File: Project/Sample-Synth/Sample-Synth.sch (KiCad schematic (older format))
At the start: 0 parts

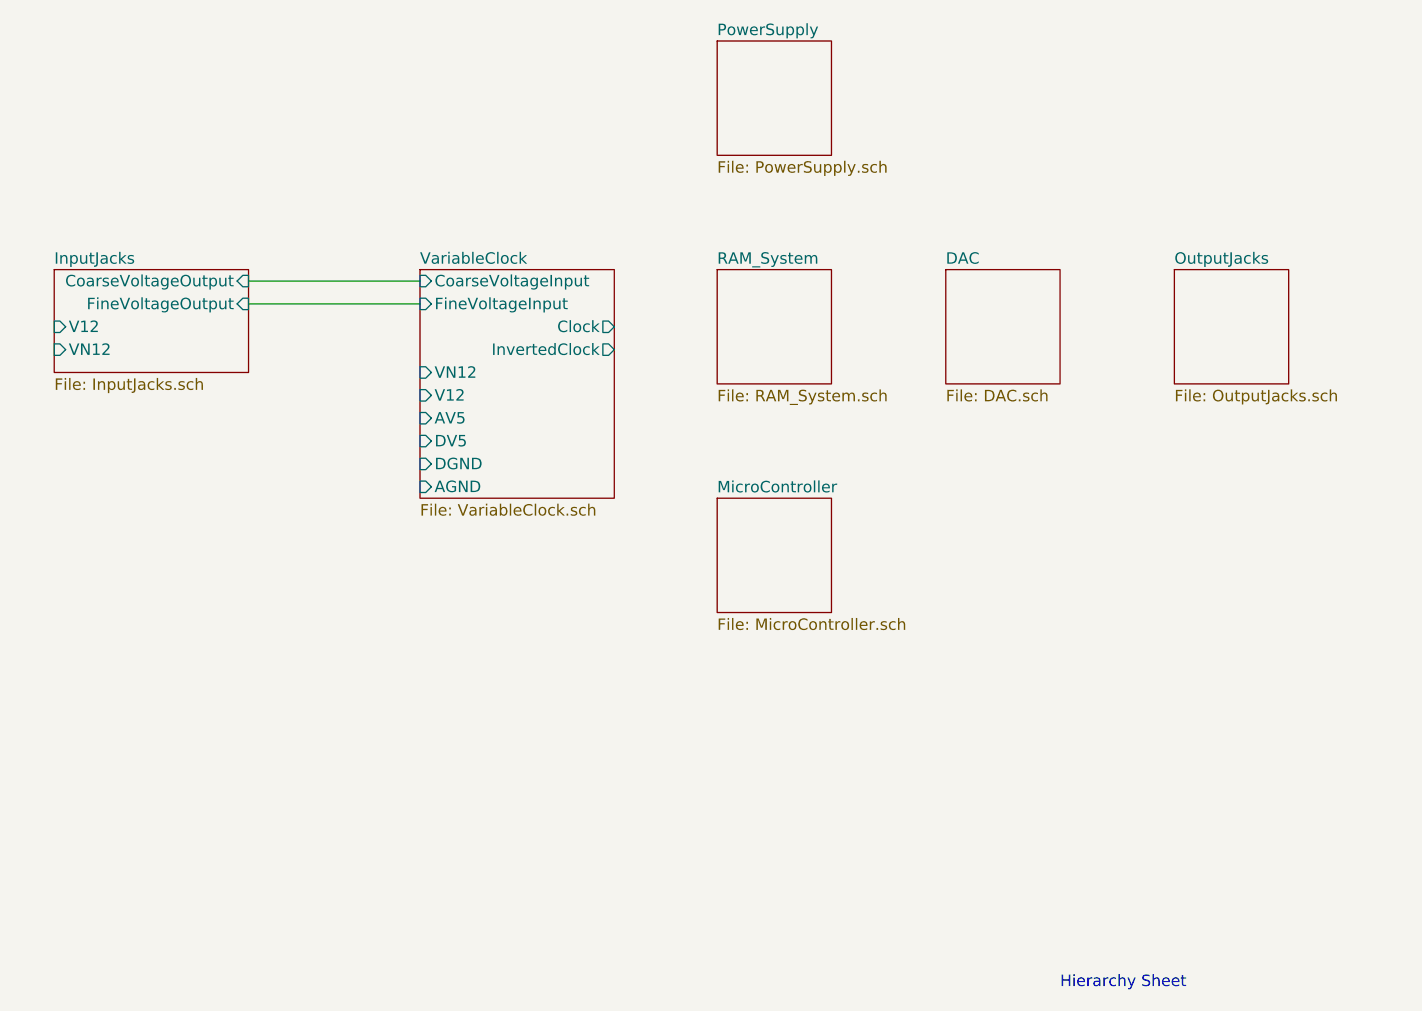
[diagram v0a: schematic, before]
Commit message: Updates to Schematic
Schematic updates: fixed connections on RAM, started setup for DAC stage.
Also swapped out the datasheet for the RAM to a more accurate one.
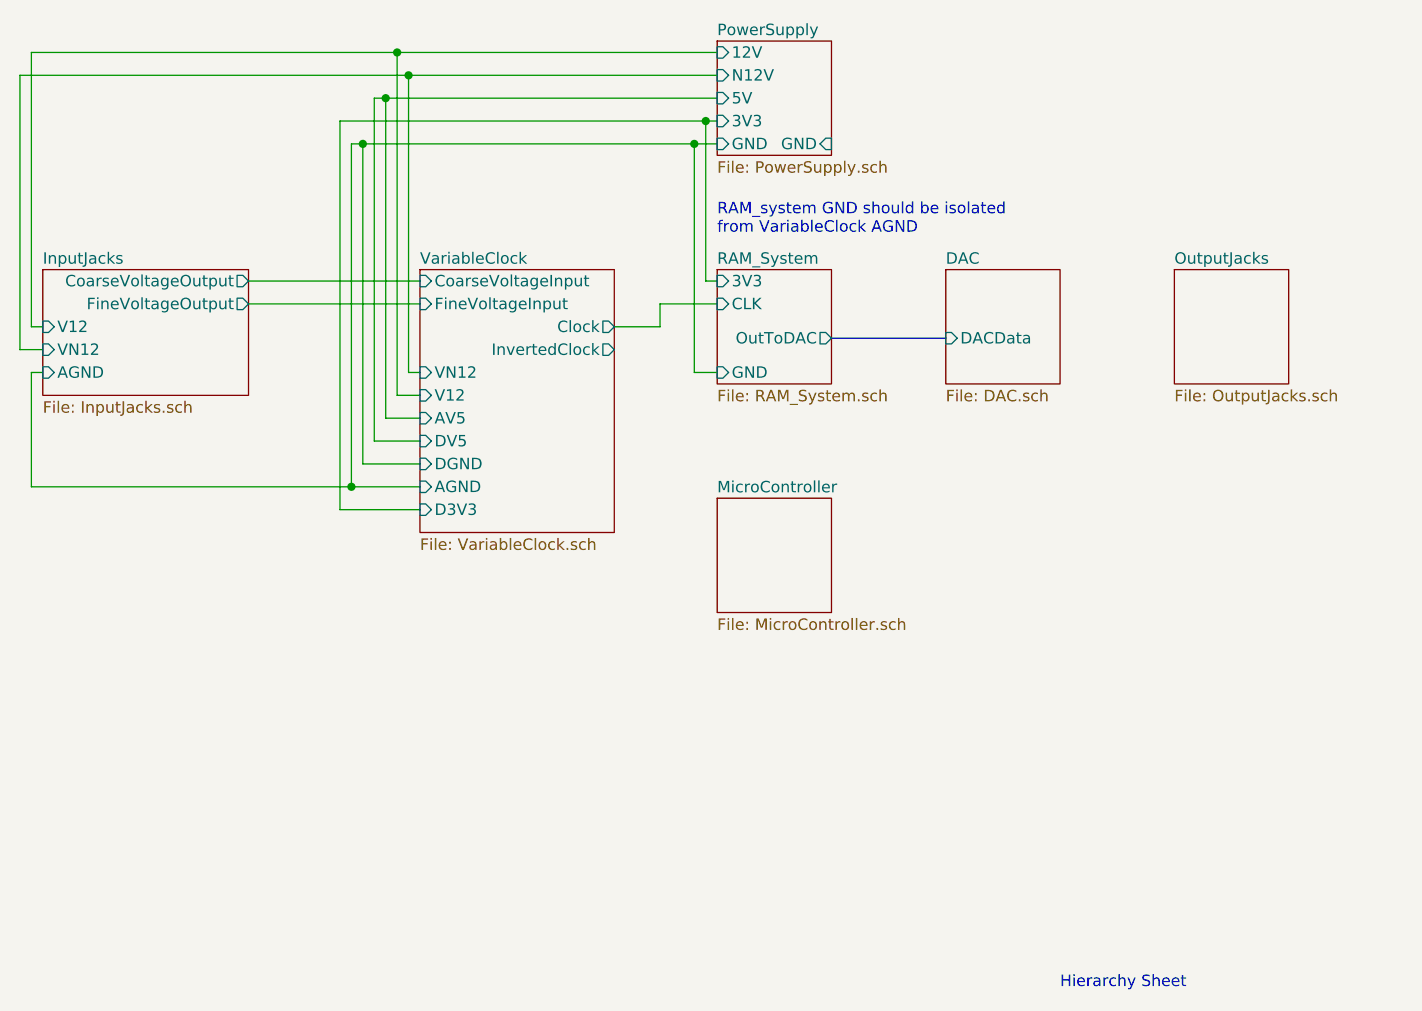
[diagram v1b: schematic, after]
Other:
- note added: "RAM_system GND should be isolated\nfrom VariableClock AGND"
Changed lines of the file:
@@
 $EndDescr
-$Sheet
-S 5500 3500 500  500
-U 60A84B2F
-F0 "RAM_System" 50
-F1 "RAM_System.sch" 50
-$EndSheet
 $Sheet
 S 5500 4500 500  500
@@
 F0 "DAC" 50
 F1 "DAC.sch" 50
+F2 "DACData" I L 6500 3800 50
 $EndSheet
 $Sheet
@@
 F0 "PowerSupply" 50
 F1 "PowerSupply.sch" 50
+F2 "12V" I L 5500 2550 50
+F3 "N12V" I L 5500 2650 50
+F4 "GND" I R 6000 2950 50
+F5 "GND" I L 5500 2950 50
+F6 "5V" I L 5500 2750 50
+F7 "3V3" I L 5500 2850 50
 $EndSheet
 $Sheet
@@
 Hierarchy Sheet
 $Sheet
-S 2600 3500 850  450
+S 2550 3500 900  550
 U 60AC03A1
 F0 "InputJacks" 50
 F1 "InputJacks.sch" 50
-F2 "CoarseVoltageOutput" I R 3450 3550 50
-F3 "FineVoltageOutput" I R 3450 3650 50
-F4 "V12" I L 2600 3750 50
-F5 "VN12" I L 2600 3850 50
+F2 "CoarseVoltageOutput" O R 3450 3550 50
+F3 "FineVoltageOutput" O R 3450 3650 50
+F4 "V12" I L 2550 3750 50
+F5 "VN12" I L 2550 3850 50
+F6 "AGND" I L 2550 3950 50
 $EndSheet
 $Sheet
-S 4200 3500 850  1000
+S 4200 3500 850  1150
 U 60A84A0D
 F0 "VariableClock" 50
@@
 F10 "AV5" I L 4200 4150 50
 F11 "DV5" I L 4200 4250 50
+F12 "D3V3" I L 4200 4550 50
 $EndSheet
 Wire Wire Line
@@
 Wire Wire Line
 	3450 3650 4200 3650
+Wire Wire Line
+	4000 4250 4200 4250
+Wire Wire Line
+	2500 2550 2500 3750
+Wire Wire Line
+	2500 3750 2550 3750
+Wire Wire Line
+	2450 2650 2450 3850
+Wire Wire Line
+	2450 3850 2550 3850
+Wire Wire Line
+	2550 3950 2500 3950
+Wire Wire Line
+	2450 2650 4150 2650
+Wire Wire Line
+	2500 2550 4100 2550
+Wire Wire Line
+	4200 4350 3950 4350
+Wire Wire Line
+	3950 4350 3950 2950
+Wire Wire Line
+	3950 2950 5400 2950
+Wire Wire Line
+	3900 4450 3900 2950
+Wire Wire Line
+	3900 2950 3950 2950
+Connection ~ 3900 4450
+Wire Wire Line
+	3900 4450 4200 4450
+Connection ~ 3950 2950
+Wire Wire Line
+	4000 4250 4000 2750
+Wire Wire Line
+	4200 4150 4050 4150
+Wire Wire Line
+	4050 4150 4050 2750
+Connection ~ 4050 2750
+Wire Wire Line
+	4050 2750 4000 2750
+Wire Wire Line
+	4200 4050 4100 4050
+Wire Wire Line
+	4100 4050 4100 2550
+Connection ~ 4100 2550
+Wire Wire Line
+	4100 2550 5500 2550
+Wire Wire Line
+	4200 3950 4150 3950
+Wire Wire Line
+	4150 3950 4150 2650
+Connection ~ 4150 2650
+Wire Wire Line
+	4150 2650 5500 2650
+Wire Wire Line
+	2500 3950 2500 4450
+Wire Wire Line
+	2500 4450 3900 4450
+Wire Wire Line
+	5500 3550 5450 3550
+Wire Wire Line
+	5500 3650 5250 3650
+Wire Wire Line
+	5250 3650 5250 3750
+Wire Wire Line
+	5250 3750 5050 3750
+Wire Wire Line
+	5500 3950 5400 3950
+Wire Wire Line
+	5400 3950 5400 2950
+Connection ~ 5400 2950
+Wire Wire Line
+	5400 2950 5500 2950
+Text Notes 5500 3350 0    50   ~ 0
+RAM_system GND should be isolated\nfrom VariableClock AGND
+Wire Wire Line
+	5500 2850 5450 2850
+Wire Wire Line
+	3850 2850 3850 4550
+Wire Wire Line
+	3850 4550 4200 4550
+$Sheet
+S 5500 3500 500  500
+U 60A84B2F
+F0 "RAM_System" 50
+F1 "RAM_System.sch" 50
+F2 "GND" I L 5500 3950 50
+F3 "3V3" I L 5500 3550 50
+F4 "CLK" I L 5500 3650 50
+F5 "OutToDAC" O R 6000 3800 50
+$EndSheet
+Wire Wire Line
+	4050 2750 5500 2750
+Wire Wire Line
+	5450 2850 5450 3550
+Connection ~ 5450 2850
+Wire Wire Line
+	5450 2850 3850 2850
+Wire Bus Line
+	6000 3800 6500 3800
 $EndSCHEMATC
